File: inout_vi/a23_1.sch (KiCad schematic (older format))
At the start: 39 parts, among them U22004 74HC02, U23001 74HC27, U23002 74LVC07, U23003 74HC04, U23004 74HC02, U23005 74HC27, U23006 74HC27, U23007 74HC02, U23008 74HC02, U23009 74HC27, U23010 74HC27, U23011 74HC02, U23012 74HC02, U23013 74HC27, U23014 74HC27, U23015 74HC27, U23016 74HC02, U23017 74HC27, U23018 74HC04, U23019 74HC02, U23020 74HC02, U23021 74HC02, U23022 74HC27, U23023 74HC27, U23024 74HC27, U23025 74HC02, U23026 74HC27, U23027 74HC02, U23028 74HC02, U23029 74HC02, U23030 74HC27, U23054 74HC04, U23056 74HC02, U23057 74HC27, U23058 74HC04, U23059 74HC02, U23060 74HC02

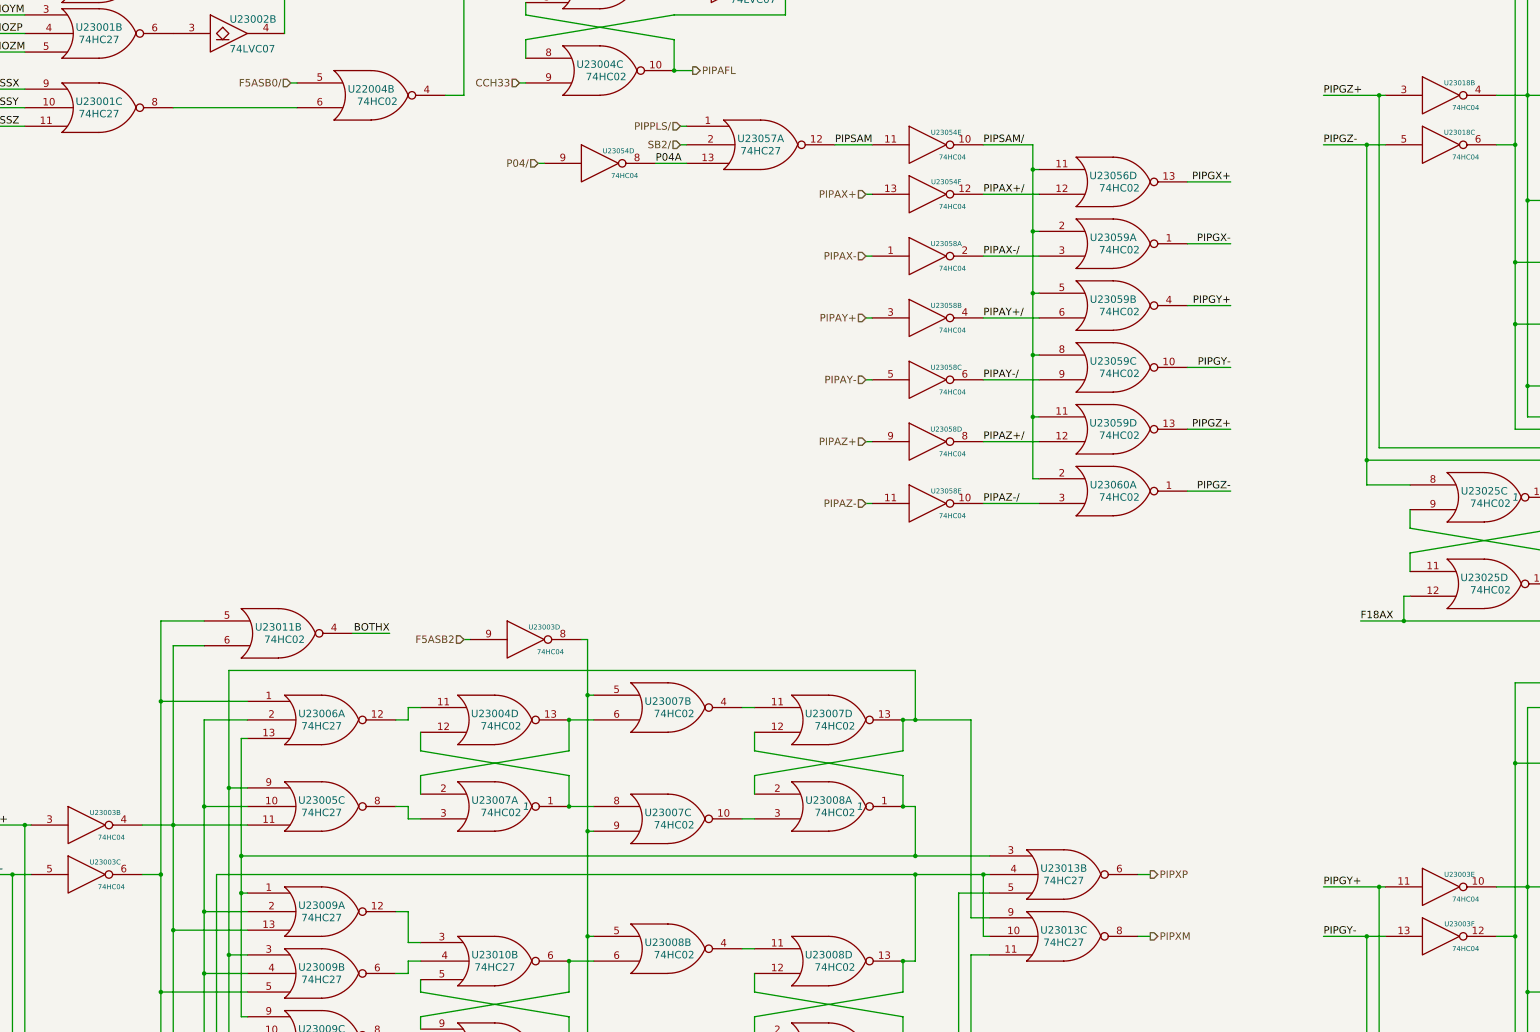
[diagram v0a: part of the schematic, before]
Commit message: Lots of initial conditions, some missed gates, and some wiring fixes
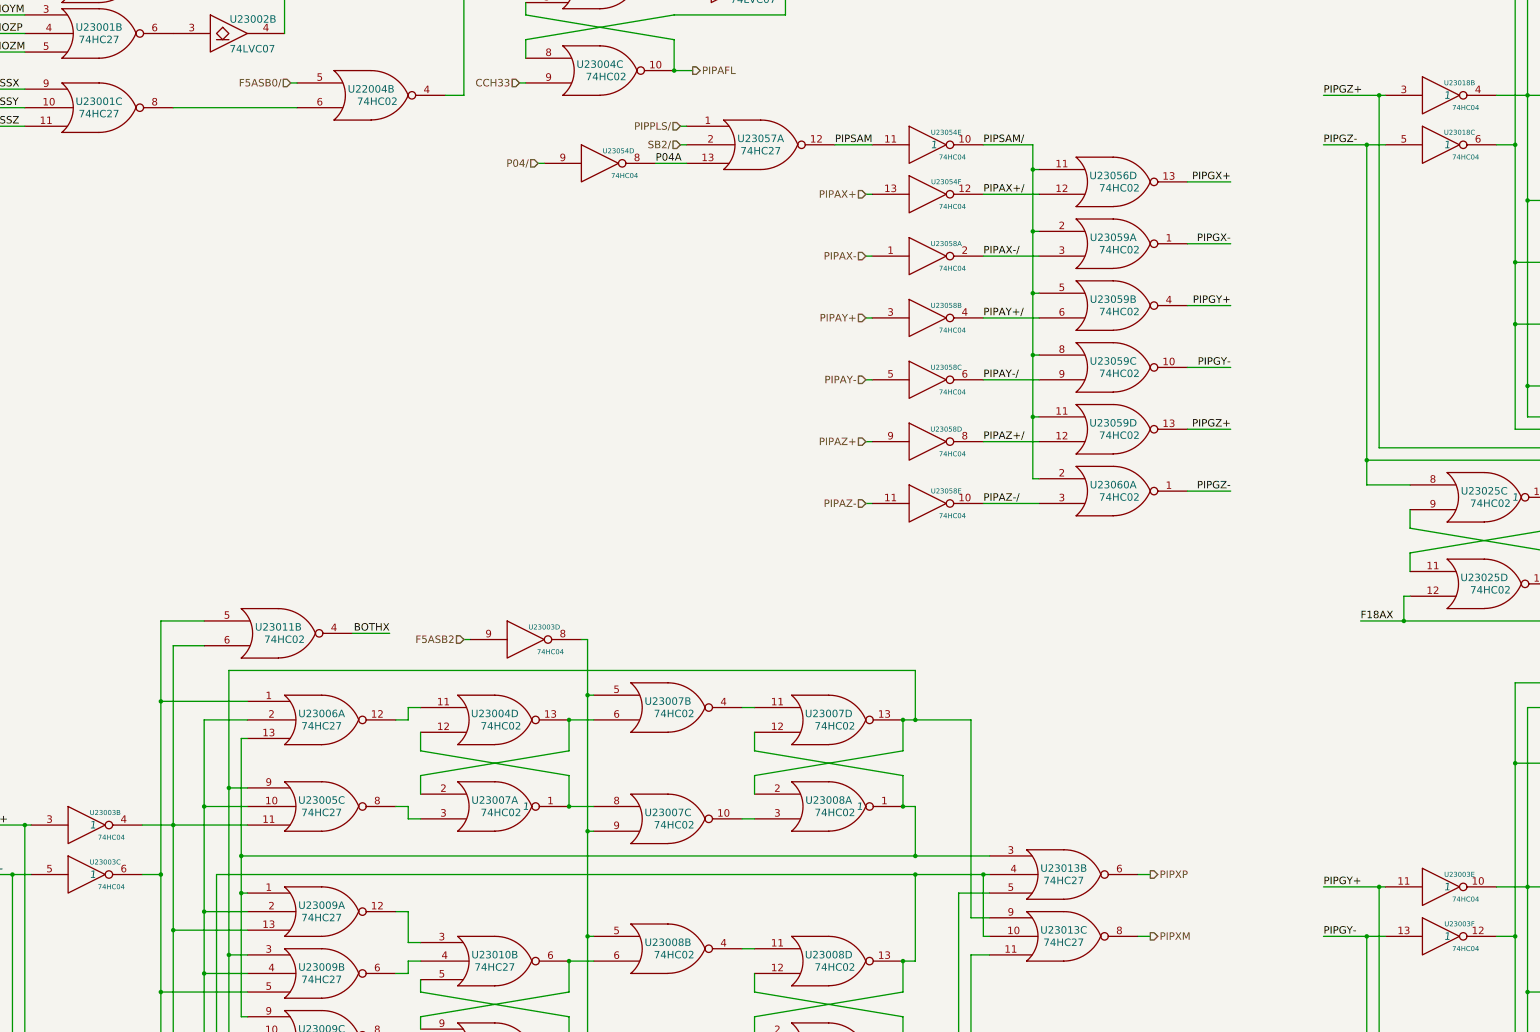
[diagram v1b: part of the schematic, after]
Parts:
- U23003, U23018, U23054: Initial (none) -> 1
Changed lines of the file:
@@
 F 2 "" H 2050 8800 60  0000 C CNN
 F 3 "" H 2050 8800 60  0000 C CNN
+F 4 "1" H 2100 8800 60  0000 C CIN "Initial"
 	2    2050 8800
 	1    0    0    -1
@@
 F 2 "" H 2050 9200 60  0000 C CNN
 F 3 "" H 2050 9200 60  0000 C CNN
+F 4 "1" H 2100 9200 60  0000 C CIN "Initial"
 	3    2050 9200
 	1    0    0    -1
@@
 F 2 "" H 13000 9300 60  0000 C CNN
 F 3 "" H 13000 9300 60  0000 C CNN
+F 4 "1" H 13050 9300 60  0000 C CIN "Initial"
 	5    13000 9300
 	1    0    0    -1
@@
 F 2 "" H 13000 9700 60  0000 C CNN
 F 3 "" H 13000 9700 60  0000 C CNN
+F 4 "1" H 13050 9700 60  0000 C CIN "Initial"
 	6    13000 9700
 	1    0    0    -1
@@
 F 2 "" H 13000 2900 60  0000 C CNN
 F 3 "" H 13000 2900 60  0000 C CNN
+F 4 "1" H 13050 2900 60  0000 C CIN "Initial"
 	2    13000 2900
 	1    0    0    -1
@@
 F 2 "" H 13000 3300 60  0000 C CNN
 F 3 "" H 13000 3300 60  0000 C CNN
+F 4 "1" H 13050 3300 60  0000 C CIN "Initial"
 	3    13000 3300
 	1    0    0    -1
@@
 F 2 "" H 8850 3300 60  0000 C CNN
 F 3 "" H 8850 3300 60  0000 C CNN
+F 4 "1" H 8900 3300 60  0000 C CIN "Initial"
 	5    8850 3300
 	1    0    0    -1

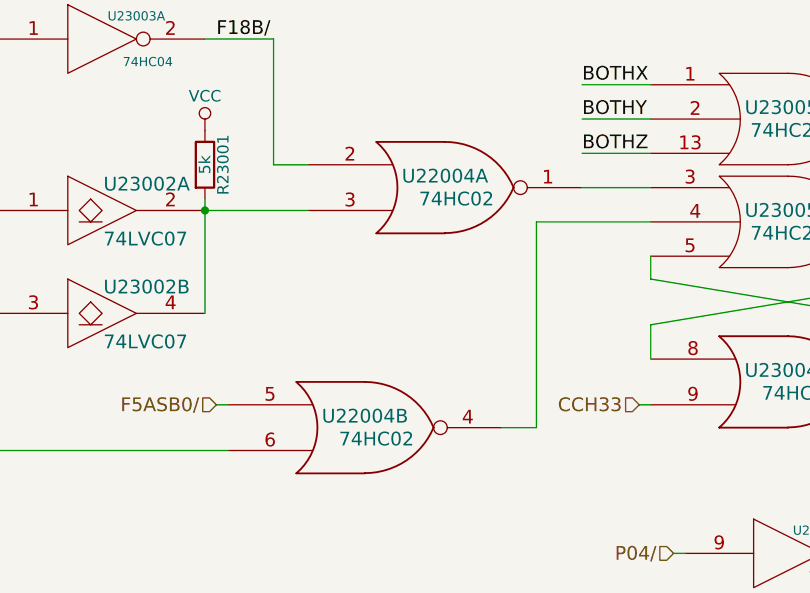
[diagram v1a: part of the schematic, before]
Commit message: Corrected some bad part identifiers
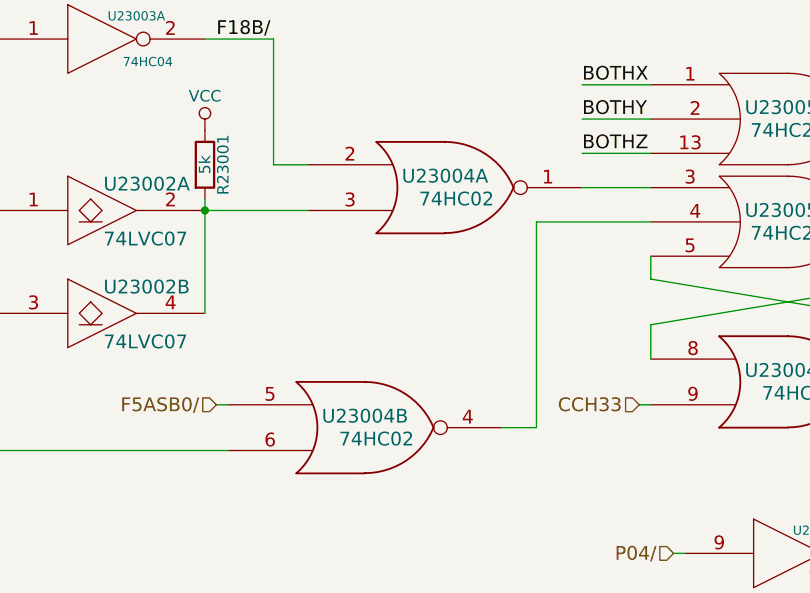
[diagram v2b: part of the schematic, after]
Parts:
- renumbered U22004 to U23004
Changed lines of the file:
@@
 F18B
 $Comp
-L 74HC02 U22004
+L 74HC02 U23004
 U 1 1 57417E65
 P 4700 1850
-F 0 "U22004" H 4700 1900 60  0000 C CNN
+F 0 "U23004" H 4700 1900 60  0000 C CNN
 F 1 "74HC02" H 4750 1800 60  0000 C CNN
 F 2 "" H 4700 1850 60  0000 C CNN
@@
 MISSZ
 $Comp
-L 74HC02 U22004
+L 74HC02 U23004
 U 2 1 574180C0
 P 4350 2900
-F 0 "U22004" H 4350 2950 60  0000 C CNN
+F 0 "U23004" H 4350 2950 60  0000 C CNN
 F 1 "74HC02" H 4400 2850 60  0000 C CNN
 F 2 "" H 4350 2900 60  0000 C CNN

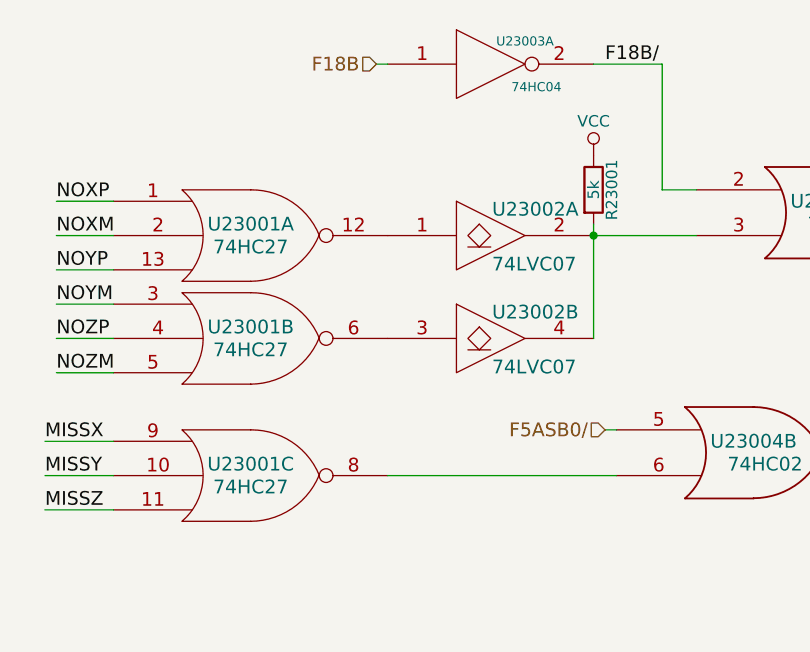
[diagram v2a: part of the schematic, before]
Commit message: Some initial condition updates to fix a couple oscillating signals I found
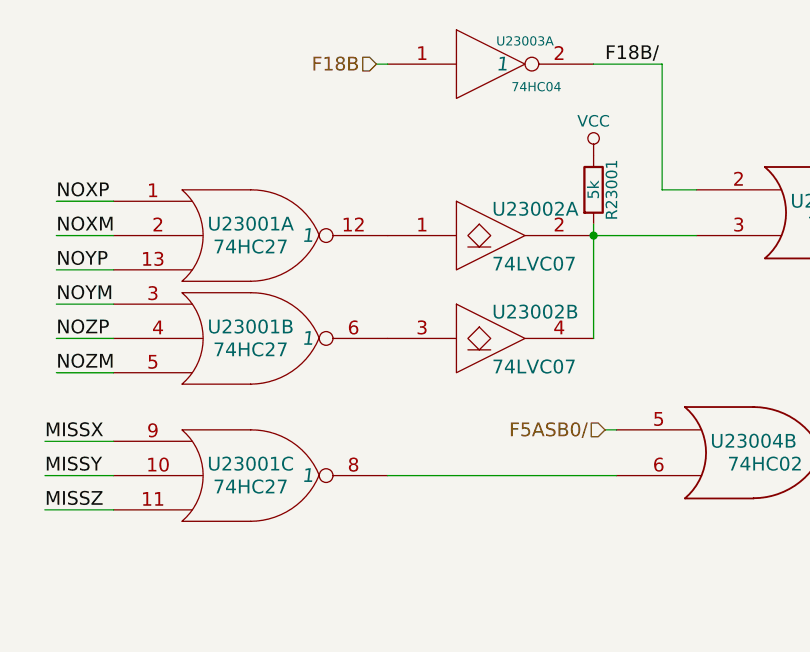
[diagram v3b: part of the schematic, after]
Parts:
- U23001, U23003: Initial (none) -> 1
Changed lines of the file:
@@
 F 2 "" H 2150 1950 60  0000 C CNN
 F 3 "" H 2150 1950 60  0000 C CNN
+F 4 "1" H 2400 1950 60  0000 C CIN "Initial"
 	1    2150 1950
 	1    0    0    -1
@@
 F 2 "" H 2150 2400 60  0000 C CNN
 F 3 "" H 2150 2400 60  0000 C CNN
+F 4 "1" H 2400 2400 60  0000 C CIN "Initial"
 	2    2150 2400
 	1    0    0    -1
@@
 F 2 "" H 3200 1200 60  0000 C CNN
 F 3 "" H 3200 1200 60  0000 C CNN
+F 4 "1" H 3250 1200 60  0000 C CIN "Initial"
 	1    3200 1200
 	1    0    0    -1
@@
 F 2 "" H 2150 3000 60  0000 C CNN
 F 3 "" H 2150 3000 60  0000 C CNN
+F 4 "1" H 2400 3000 60  0000 C CIN "Initial"
 	3    2150 3000
 	1    0    0    -1

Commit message: Fixed not->1-input nor in the rest of the modules.
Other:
- moved on the sheet: U23003A, U23003B, U23003C, U23003D, U23003E, U23003F, U23011B, U23012D, U23018A, U23018B, U23018C, U23018D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

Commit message: Updated Inout VI to be on +4VSW
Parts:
- renumbered U23054 to U23053, U23056 to U23055, U23057 to U23056, U23058 to U23057, U23059 to U23058, U23060 to U23059
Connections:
- net labels added: +4VSW
- net labels removed: VCC
